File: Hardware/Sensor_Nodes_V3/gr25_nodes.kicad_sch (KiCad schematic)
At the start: 10 parts, among them U1 STM32G474RETx, U2 TPS563200

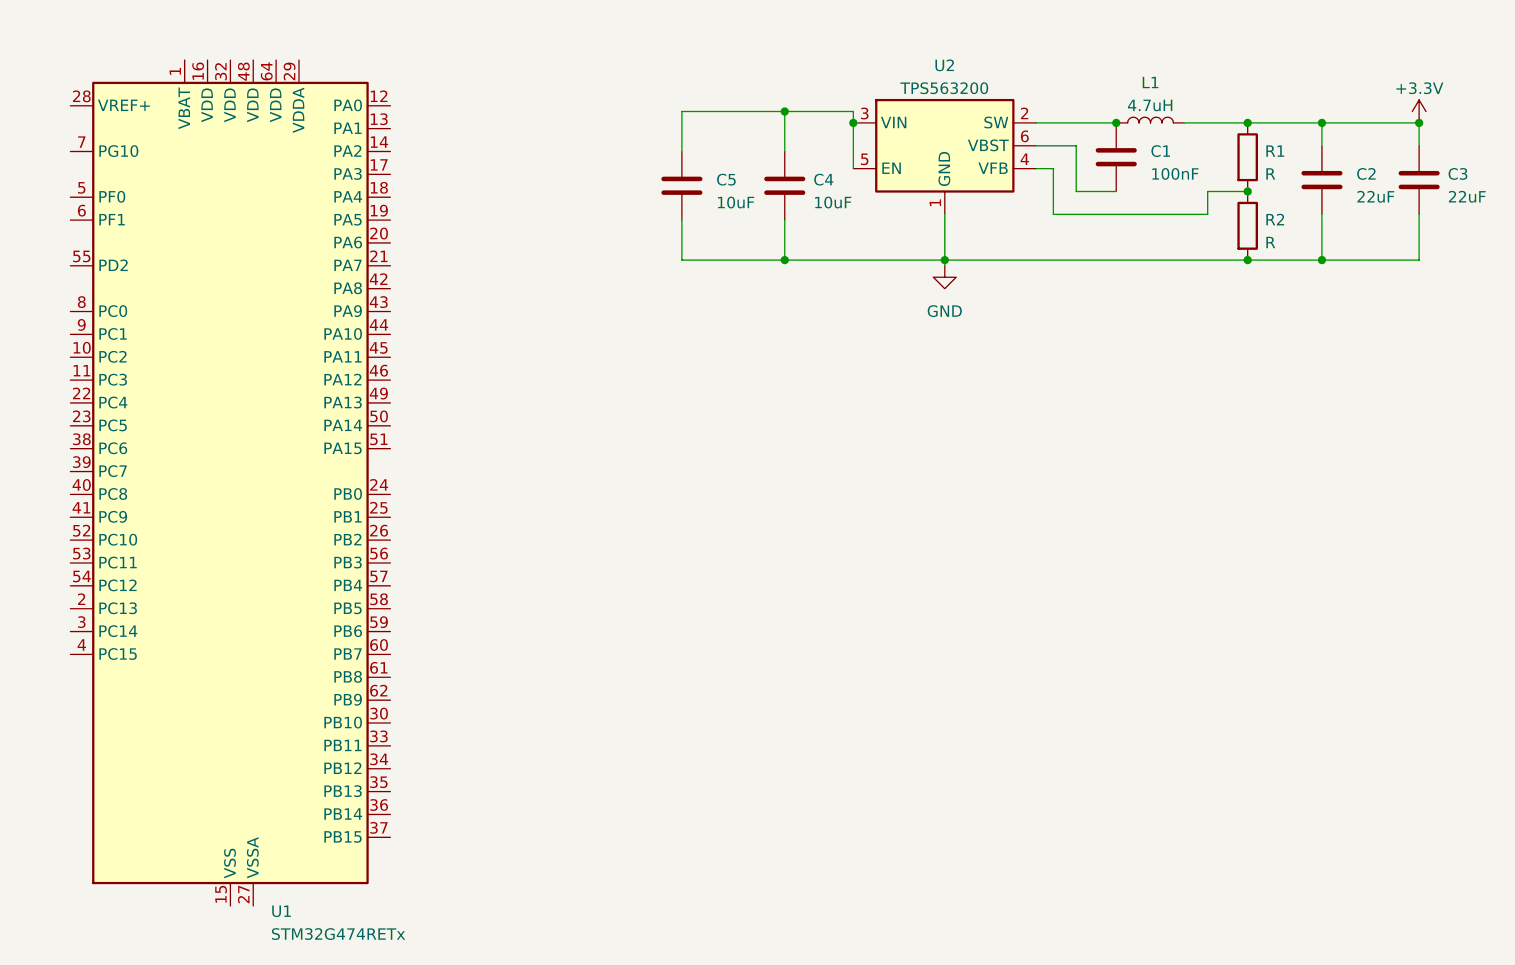
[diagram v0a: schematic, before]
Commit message: added some v3 work, mostly stlink on pcb and power stuff on main MCU
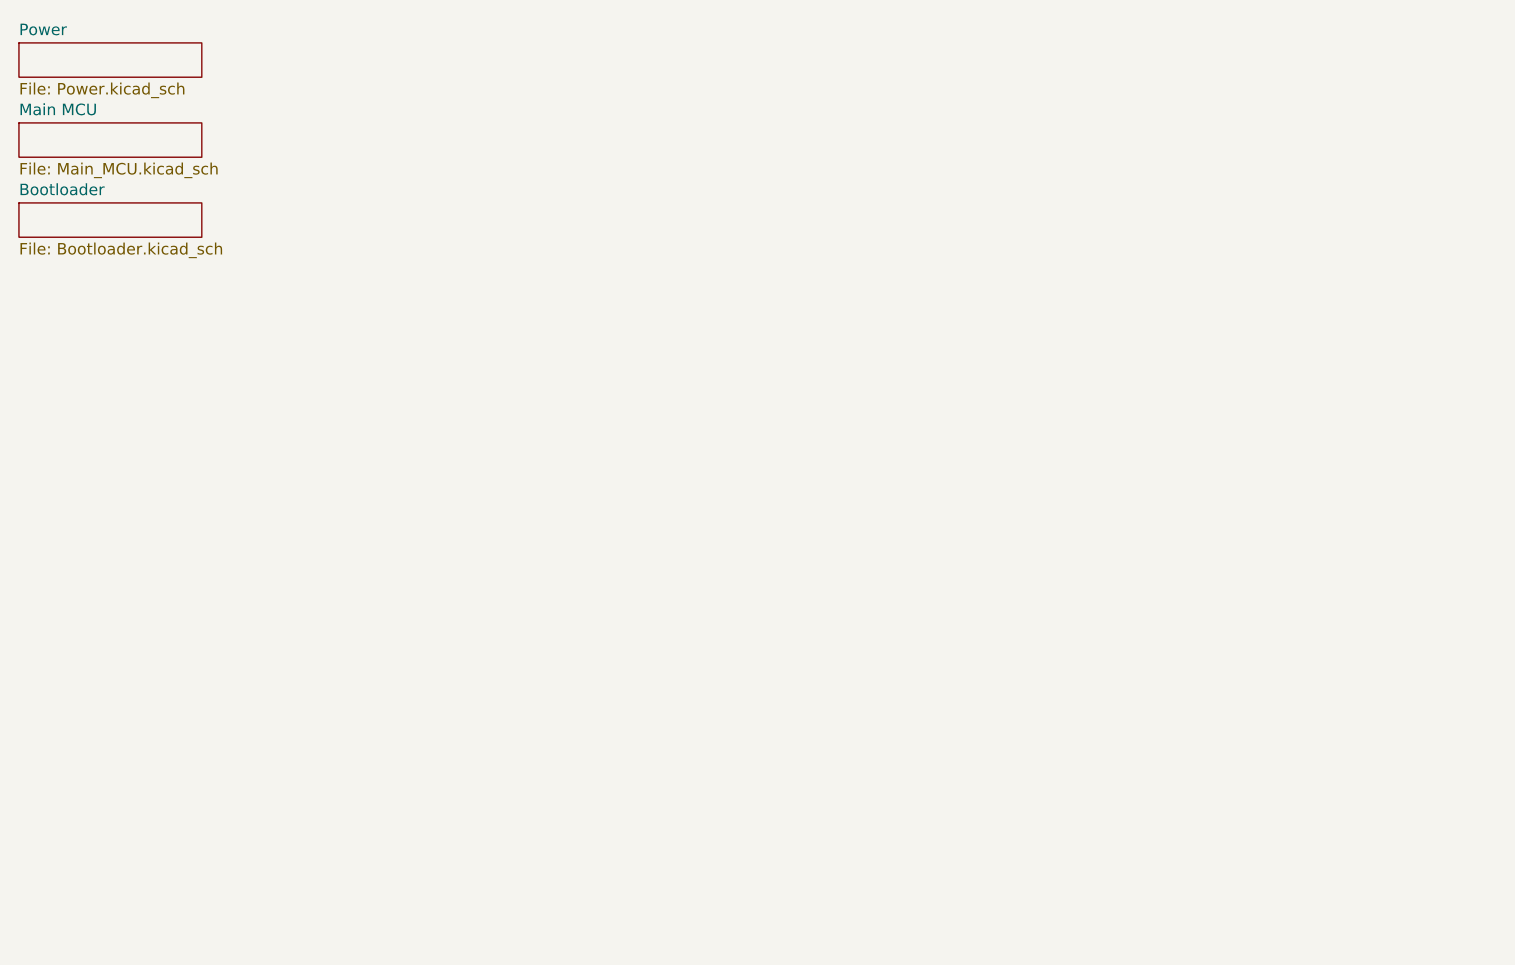
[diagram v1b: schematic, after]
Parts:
- removed C1: 100nF, symbol Device:C
- removed C2, C3: 22uF, symbol Device:C
- removed C4, C5: 10uF, symbol Device:C
- removed L1: 4.7uH, symbol Device:L
- removed R1, R2: R, symbol Device:R
- removed U1: STM32G474RETx, Package_QFP:LQFP-64_10x10mm_P0.5mm, symbol MCU_ST_STM32G4:STM32G474RETx
- removed U2: TPS563200, Package_TO_SOT_SMD:SOT-23-6, symbol Regulator_Switching:TPS563200
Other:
- added sheet Bootloader (Bootloader.kicad_sch)
- added sheet Main MCU (Main_MCU.kicad_sch)
- added sheet Power (Power.kicad_sch)

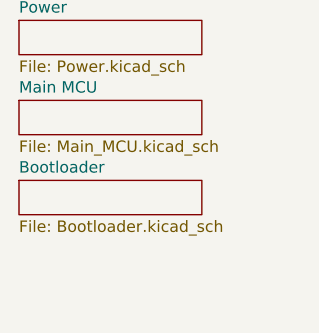
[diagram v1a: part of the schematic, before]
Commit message: alt placement made
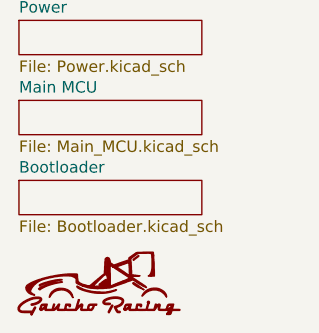
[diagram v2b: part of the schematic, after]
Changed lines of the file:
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@@
 	(generator_version "8.0")
 	(paper "A4")
+	(symbol
+		(lib_id "logo:LOGO")
+		(at 25.4 45.72 0)
+		(unit 1)
+		(exclude_from_sim no)
+		(in_bom yes)
+		(on_board yes)
+		(dnp no)
+		(fields_autoplaced yes)
+		(property "Reference" "#G1"
+			(at 25.4 42.8424 0)
+			(effects
+				(font
+					(size 1.27 1.27)
+				)
+				(hide yes)
+			)
+		)
+		(property "Value" "LOGO"
+			(at 25.4 48.5976 0)
+			(effects
+				(font
+					(size 1.27 1.27)
+				)
+				(hide yes)
+			)
+		)
+		(property "Footprint" "Logo:grloho"
+			(at 25.4 45.72 0)
+			(effects
+				(font
+					(size 1.27 1.27)
+				)
+				(hide yes)
+			)
+		)
+		(property "Datasheet" ""
+			(at 25.4 45.72 0)
+			(effects
+				(font
+					(size 1.27 1.27)
+				)
+				(hide yes)
+			)
+		)
+		(property "Description" ""
+			(at 25.4 45.72 0)
+			(effects
+				(font
+					(size 1.27 1.27)
+				)
+				(hide yes)
+			)
+		)
+		(instances
+			(project ""
+				(path "/7b4e8e38-4440-451f-8c12-a5c49d6e3525"
+					(reference "#G1")
+					(unit 1)
+				)
+			)
+		)
+	)
 	(sheet
 		(at 16.51 25.4)
